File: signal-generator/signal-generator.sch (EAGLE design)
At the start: 0 parts

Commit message: added signal generator
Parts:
- added C1, C2, C3, C4: (no value), rcl:C-USC0805
- added IC1: LM324D, linear:LM324D
- added R1, R2, R3, R4, RB1, RB2, RF, RG: (no value), rcl:R-US_R0805
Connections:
- new net GND: C1.2, C2.2, C3.2, C4.2, IC1P.V-, RB2.1
- new net N$1: IC1A.-IN, RF.1, RG.2
- new net N$2: IC1B.-IN, IC1B.OUT, R2.1
- new net N$3: C1.1, IC1B.+IN, R1.2
- new net N$4: IC1D.-IN, IC1D.OUT, R3.2
- new net N$5: C2.1, IC1D.+IN, R2.2
- new net N$6: C4.1, R4.1, RG.1
- new net N$8: IC1A.OUT, R1.1, RF.2
- new net N$9: C3.1, IC1C.+IN, R3.1
- new net VDD: IC1P.V+, RB1.2
- new net VOUT: IC1C.-IN, IC1C.OUT, R4.2
- new net VREF: IC1A.+IN, RB1.1, RB2.2

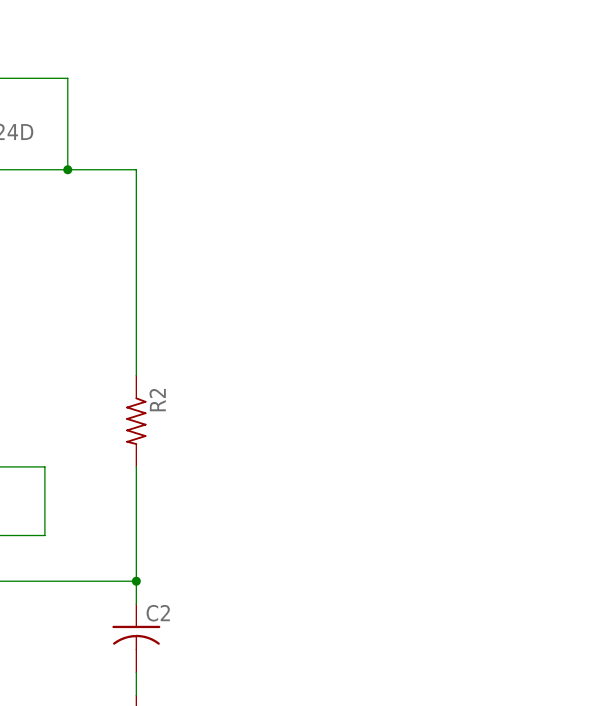
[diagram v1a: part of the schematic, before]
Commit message: added pins to signal generator
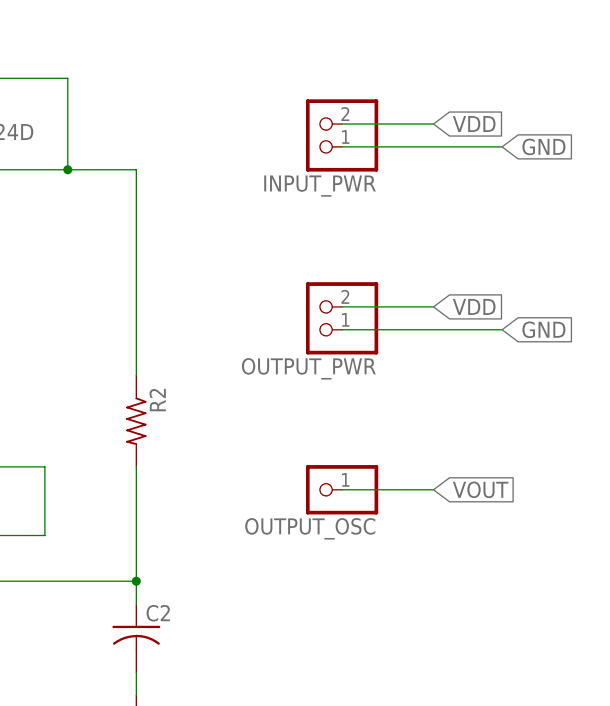
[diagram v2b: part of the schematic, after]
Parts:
- added INPUT_PWR, OUTPUT_PWR: (no value), pinhead:PINHD-1X2/90
- added OUTPUT_OSC: (no value), pinhead:PINHD-1X1
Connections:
- net GND: now also INPUT_PWR.1, OUTPUT_PWR.1
- net VDD: now also INPUT_PWR.2, OUTPUT_PWR.2
- net VOUT: now also OUTPUT_OSC.1
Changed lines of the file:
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@@
 <part name="RB2" library="rcl" deviceset="R-US_" device="R0805"/>
 <part name="GND6" library="supply1" deviceset="GND" device=""/>
+<part name="INPUT_PWR" library="pinhead" deviceset="PINHD-1X2" device="/90"/>
+<part name="OUTPUT_PWR" library="pinhead" deviceset="PINHD-1X2" device="/90"/>
+<part name="OUTPUT_OSC" library="pinhead" deviceset="PINHD-1X1" device=""/>
 </parts>
 <sheets>
@@
 <instance part="RB2" gate="G$1" x="-66.04" y="10.16" rot="R90"/>
 <instance part="GND6" gate="1" x="-66.04" y="0"/>
+<instance part="INPUT_PWR" gate="G$1" x="99.06" y="73.66" rot="R180"/>
+<instance part="OUTPUT_PWR" gate="G$1" x="99.06" y="53.34" rot="R180"/>
+<instance part="OUTPUT_OSC" gate="G$1" x="99.06" y="33.02" rot="R180"/>
 </instances>
 <busses>
@@
 <label x="-15.24" y="40.64" size="1.778" layer="95" rot="R180" xref="yes"/>
 </segment>
+<segment>
+<pinref part="OUTPUT_OSC" gate="G$1" pin="1"/>
+<wire x1="101.6" y1="33.02" x2="111.76" y2="33.02" width="0.1524" layer="91"/>
+<label x="111.76" y="33.02" size="1.778" layer="95" xref="yes"/>
+</segment>
 </net>
 <net name="N$8" class="0">
@@
 <wire x1="-66.04" y1="2.54" x2="-66.04" y2="5.08" width="0.1524" layer="91"/>
 </segment>
+<segment>
+<pinref part="INPUT_PWR" gate="G$1" pin="1"/>
+<wire x1="101.6" y1="71.12" x2="119.38" y2="71.12" width="0.1524" layer="91"/>
+<label x="119.38" y="71.12" size="1.778" layer="95" xref="yes"/>
+</segment>
+<segment>
+<pinref part="OUTPUT_PWR" gate="G$1" pin="1"/>
+<label x="119.38" y="50.8" size="1.778" layer="95" xref="yes"/>
+<wire x1="101.6" y1="50.8" x2="119.38" y2="50.8" width="0.1524" layer="91"/>
+</segment>
 </net>
 <net name="N$3" class="0">
@@
 <label x="-63.5" y="35.56" size="1.778" layer="95" xref="yes"/>
 </segment>
-</net>
+<segment>
+<pinref part="INPUT_PWR" gate="G$1" pin="2"/>
+<wire x1="101.6" y1="73.66" x2="111.76" y2="73.66" width="0.1524" layer="91"/>
+<label x="111.76" y="73.66" size="1.778" layer="95" xref="yes"/>
+</segment>
+<segment>
+<pinref part="OUTPUT_PWR" gate="G$1" pin="2"/>
+<wire x1="101.6" y1="53.34" x2="111.76" y2="53.34" width="0.1524" layer="91"/>
+<label x="111.76" y="53.34" size="1.778" layer="95" xref="yes"/>
+</segment>
+</net>
